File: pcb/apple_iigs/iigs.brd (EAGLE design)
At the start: 81 x 45 mm, 16 parts, among them J1 ATX24RH

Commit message: added iigs
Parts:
- removed C1, C2: (no value), capacitor-wima:C5B2.5
- removed JP3: (no value), appleii:1X04
- removed U$3: ROCK_SW, atx4vc:ROCK_SWITCH
- removed U$6: APPLEII, atx4vc:APPLEII
- added JP2: (no value), pinhead:1X03
- J1: device macse:ATX24_RIGHT_ANGLE -> appleii:ATX24_RIGHT_ANGLE
- moved J7 39.5 mm to (21.6, 4.23), turned to 0 degrees
- moved JP1 31.3 mm to (34.3, 5.57), turned to 0 degrees
- moved J1 28.7 mm to (3.00, 15.0), turned to 270 degrees
- moved U$1 25.2 mm to (31.3, 11.7)
- moved U$2 25.2 mm to (31.3, 19.5)
- moved U$4 22.8 mm to (51.5, 11.0)
- moved U$7 22.8 mm to (57.3, 15.0)
- moved JP4 18.8 mm to (44.3, 3.62)
- moved U$5 17.9 mm to (18.0, 11.0)
- moved IC1 11.8 mm to (27.7, 29.0)
- moved C3 11.7 mm to (38.7, 26.3)
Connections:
- new net N$1: JP2.2, JP4.2
- net +12V: now also JP2.3; no longer JP3.2, U$6.4
- net +5V: now also JP2.1; no longer JP4.2, U$6.3
- net -12V: no longer U$6.5
- net -5V: no longer U$6.6
- net GND: no longer C1.2, C2.2, JP3.1, U$3.P$1, U$3.P$3, U$6.1, U$6.2
- net N$5: no longer U$3.P$2, U$3.P$4
- net N$6: no longer C1.1
- net N$8: no longer C2.1
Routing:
- net N$5: track 103.7 -> 23.4 mm
- net N$6: track 93.8 -> 46.7 mm
- net -5V: track 70.9 -> 29.8 mm
- net +5V: track 67.5 -> 36.5 mm
- net +12V: track 71.0 -> 43.4 mm
- net N$8: track 84.8 -> 60.1 mm, vias 1 -> 0
- net N$1: track 0.00 -> 4.41 mm
- net -12V: track 81.7 -> 77.6 mm
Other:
- board size 81 x 45 mm -> 60 x 52 mm
- board text added: "Apple IIgs PicoPSU Adaptor"
- board text removed: "Apple II / II Plus / IIe / IIgs PicoPSU Adaptor"
- board text removed: "picoRC.com"

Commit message: updated IIGS design
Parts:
- removed J7: (no value), atx_power_control:SCREWTERMINAL-3.5MM-2-NS
- removed U$4, U$5: M2.5_MOUNTING_HOLE, appleii:M3_MOUNTING_HOLE_PACK
- moved JP4 19.1 mm to (28.7, 14.6)
- moved U$7 17.8 mm to (43.3, 26.0)
- moved JP1 16.6 mm to (19.7, 13.5)
- moved C3 13.3 mm to (31.2, 37.3)
- moved IC1 12.9 mm to (21.4, 40.3)
- moved U$1 12.3 mm to (27.3, 23.4)
- moved U$2 11.9 mm to (27.3, 30.8)
- moved JP2 11.4 mm to (37.0, 15.6), turned to 90 degrees
- moved J1 11.0 mm to (3.00, 26.0)
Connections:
- net GND: no longer J7.2
- net N$5: no longer J7.1
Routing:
- net GND: track 0.00 -> 18.2 mm
- net N$5: track 23.4 -> 6.03 mm
- net -12V: track 77.6 -> 64.7 mm
- net +12V: track 43.4 -> 31.4 mm
- net +5V: track 36.5 -> 29.0 mm
- net -5V: track 29.8 -> 22.3 mm
- net N$8: track 60.1 -> 52.7 mm
- net N$1: track 4.41 -> 11.2 mm
- net N$6: track 46.7 -> 44.8 mm
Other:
- board size 60 x 52 mm -> 46 x 52 mm
- board text added: "1uF"
- board text added: "5A FUSE"
- board text added: "Apple IIGS PicoPSU Adaptor"
- board text added: "PD1 dekuNukem APR2023"
- board text added: "PSW"
- board text removed: "Apple IIgs PicoPSU Adaptor"
- board text removed: "FUSE 5A MAX"
- board text removed: "PS_ON"
- board text removed: "PT1 dekuNukem DEC 2022"
- board text removed: "min 1uF"

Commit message: updated silkscreen and improved GND return
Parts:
- moved JP1 0.13 mm to (19.7, 13.4), turned to 180 degrees
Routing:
- net GND: track 18.2 -> 0.00 mm
- net N$5: track 6.03 -> 9.52 mm
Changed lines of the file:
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@@
 <text x="34.5462" y="18.256" size="1.4224" layer="25" distance="35" rot="R270" align="center">12</text>
 <text x="34.576" y="12.8932" size="1.778" layer="25" distance="35" align="center">5</text>
-<text x="20.86" y="35.0692" size="1.016" layer="25" distance="35" align="center">G</text>
-<text x="23.527" y="35.0692" size="1.016" layer="25" distance="35" align="center">-12</text>
-<text x="26.067" y="35.0692" size="1.016" layer="25" distance="35" align="center">-5</text>
+<text x="18.923" y="35.179" size="1.016" layer="25" distance="35" align="center">G</text>
+<text x="21.209" y="35.179" size="1.016" layer="25" distance="35" align="center">-12</text>
+<text x="23.876" y="35.179" size="1.016" layer="25" distance="35" align="center">-5</text>
 <text x="39.672" y="17.9242" size="1.778" layer="25" distance="35" align="center">G</text>
 <text x="39.672" y="13.8602" size="1.778" layer="25" distance="35" align="center">G</text>
@@
 <text x="39.5632" y="38.892" size="1.778" layer="25" distance="35" rot="R270" align="center">-5</text>
 <text x="39.1768" y="33.781" size="1.778" layer="25" distance="35" rot="R90" align="center">-12</text>
-<text x="15.994" y="13.727" size="1.4224" layer="25" rot="R270" align="center">PSW</text>
+<text x="16.121" y="13.473" size="1.4224" layer="25" rot="R270" align="center">PSW</text>
 <wire x1="44.095" y1="11.5" x2="19.04" y2="11.5" width="0.0762" layer="20"/>
 <wire x1="19.04" y1="11.5" x2="16.5" y2="8.96" width="0.0762" layer="20" curve="90"/>
@@
 <element name="U$1" library="atx_power_control" package="FUSE_HOLDER_3IN1" value="CAR_FUSE_HOLDER3IN1" x="27.322" y="23.368" smashed="yes" rot="R180"/>
 <element name="U$2" library="atx_power_control" package="FUSE_HOLDER_3IN1" value="CAR_FUSE_HOLDER3IN1" x="27.322" y="30.768" smashed="yes"/>
-<element name="JP1" library="pinhead" library_urn="urn:adsk.eagle:library:325" package="1X02" package3d_urn="urn:adsk.eagle:package:22435/2" value="" x="19.738" y="13.52" smashed="yes">
-<attribute name="POPULARITY" value="98" x="19.738" y="13.52" size="1.778" layer="27" display="off"/>
-<attribute name="VALUE" x="17.198" y="10.345" size="1.27" layer="27"/>
+<element name="JP1" library="pinhead" library_urn="urn:adsk.eagle:library:325" package="1X02" package3d_urn="urn:adsk.eagle:package:22435/2" value="" x="19.738" y="13.393" smashed="yes" rot="R180">
+<attribute name="POPULARITY" value="98" x="19.738" y="13.393" size="1.778" layer="27" rot="R180" display="off"/>
+<attribute name="VALUE" x="22.278" y="16.568" size="1.27" layer="27" rot="R180"/>
 </element>
 <element name="J1" library="appleii" package="ATX24_RIGHT_ANGLE" value="ATX24RH" x="3" y="26" smashed="yes" rot="R270"/>
@@
 <contactref element="U$7" pad="21"/>
 <contactref element="JP4" pad="1"/>
-<wire x1="33.782" y1="36.432" x2="33.782" y2="37.321" width="1.27" layer="1"/>
-<wire x1="33.782" y1="36.432" x2="32.402" y2="35.052" width="1.27" layer="1"/>
-<wire x1="18.9022" y1="37.716" x2="18.9022" y2="36.4698" width="1.27" layer="1"/>
-<wire x1="20.32" y1="35.052" x2="32.402" y2="35.052" width="1.27" layer="1"/>
-<wire x1="18.9022" y1="36.4698" x2="20.32" y2="35.052" width="1.27" layer="1"/>
+<polygon width="0.2032" layer="1" thermals="no">
+<vertex x="17.399" y="15.494"/>
+<vertex x="17.399" y="11.684"/>
+<vertex x="19.431" y="11.684"/>
+<vertex x="19.431" y="15.494"/>
+<vertex x="17.526" y="15.494"/>
+</polygon>
+<polygon width="0.2032" layer="1" thermals="no">
+<vertex x="17.78" y="39.751"/>
+<vertex x="20.066" y="39.751"/>
+<vertex x="20.066" y="35.814"/>
+<vertex x="17.78" y="35.814"/>
+</polygon>
+<polygon width="0.2032" layer="1" thermals="no">
+<vertex x="32.258" y="38.608"/>
+<vertex x="35.306" y="38.608"/>
+<vertex x="35.306" y="36.068"/>
+<vertex x="32.258" y="36.068"/>
+</polygon>
 </signal>
 <signal name="+5V">
@@
 <contactref element="JP1" pad="1"/>
 <contactref element="J1" pad="16"/>
-<wire x1="13.26" y1="15.5" x2="14.853" y2="15.5" width="0.6096" layer="16"/>
-<wire x1="16.833" y1="13.52" x2="18.468" y2="13.52" width="0.6096" layer="16"/>
-<wire x1="14.853" y1="15.5" x2="16.833" y2="13.52" width="0.6096" layer="16"/>
+<wire x1="13.26" y1="15.5" x2="20.441" y2="15.5" width="0.3048" layer="16"/>
+<wire x1="21.008" y1="14.933" x2="21.008" y2="13.393" width="0.3048" layer="16"/>
+<wire x1="20.441" y1="15.5" x2="21.008" y2="14.933" width="0.3048" layer="16"/>
 </signal>
 <signal name="-5V">

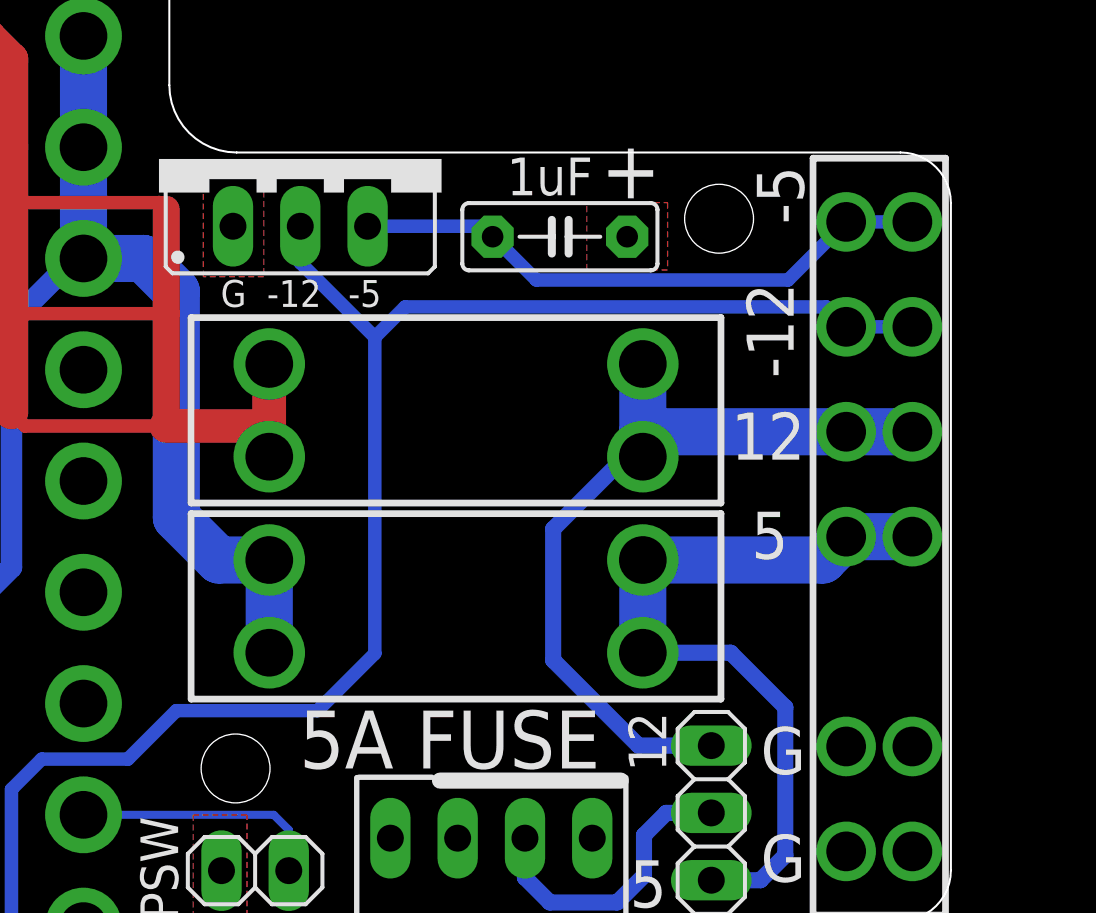
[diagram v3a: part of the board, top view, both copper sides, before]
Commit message: changed to 70L05
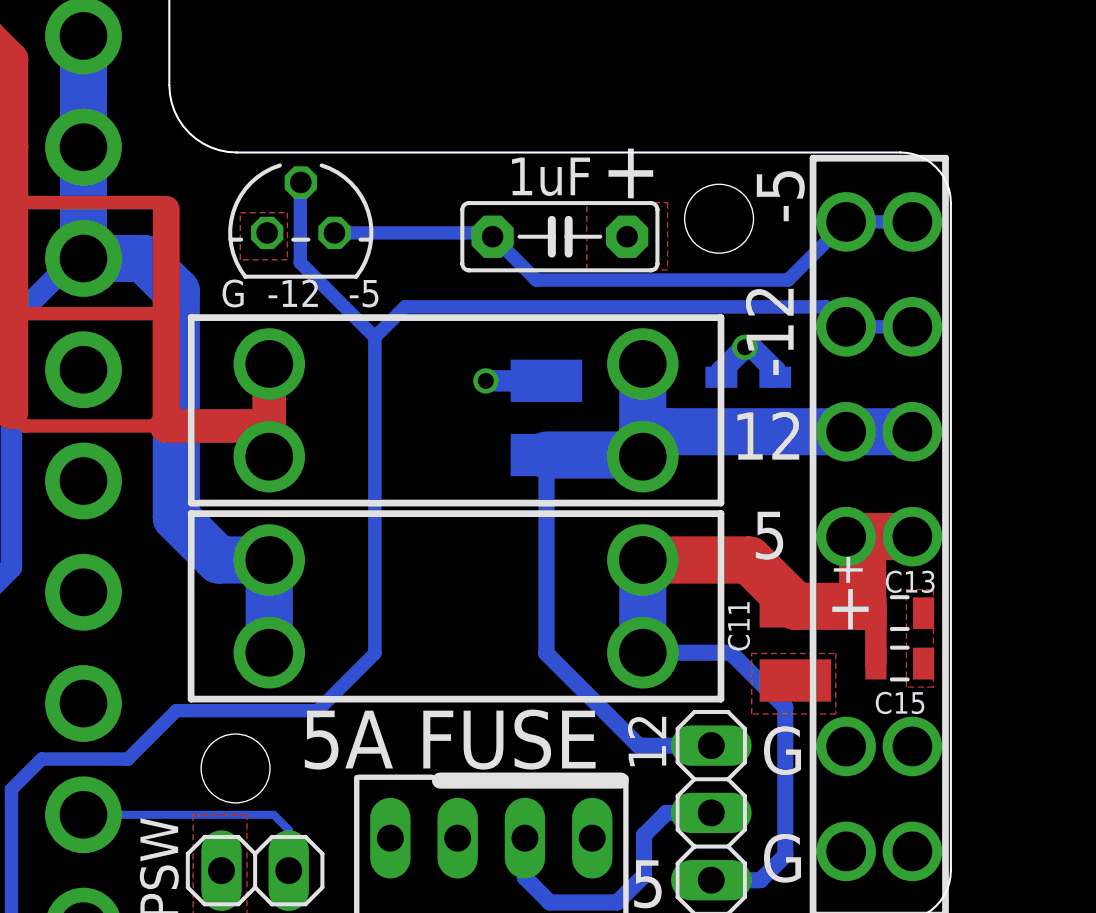
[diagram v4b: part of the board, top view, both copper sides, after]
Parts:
- removed IC1: (no value), v-reg:79XXS
- added C1, C11: 47uF, clock:C1210
- added C13, C15, C2, C4: 100nF, clock:0805@1
- added IC2: (no value), linear:TO92
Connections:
- net +12V: now also C1.1, C2.2, C4.2
- net +5V: now also C11.1, C13.2, C15.2
- net -12V: now also IC2.2; no longer IC1.IN
- net -5V: now also IC2.3; no longer IC1.OUT
- net GND: now also C1.2, C11.2, C13.1, C15.1, C2.1, C4.1, IC2.1; no longer IC1.GND
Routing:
- net +5V: track 29.0 -> 38.5 mm
- net +12V: track 31.4 -> 39.3 mm
- net GND: track 0.00 -> 5.55 mm, vias 0 -> 2
- net -12V: track 64.7 -> 66.4 mm
- net -5V: track 22.3 -> 23.5 mm

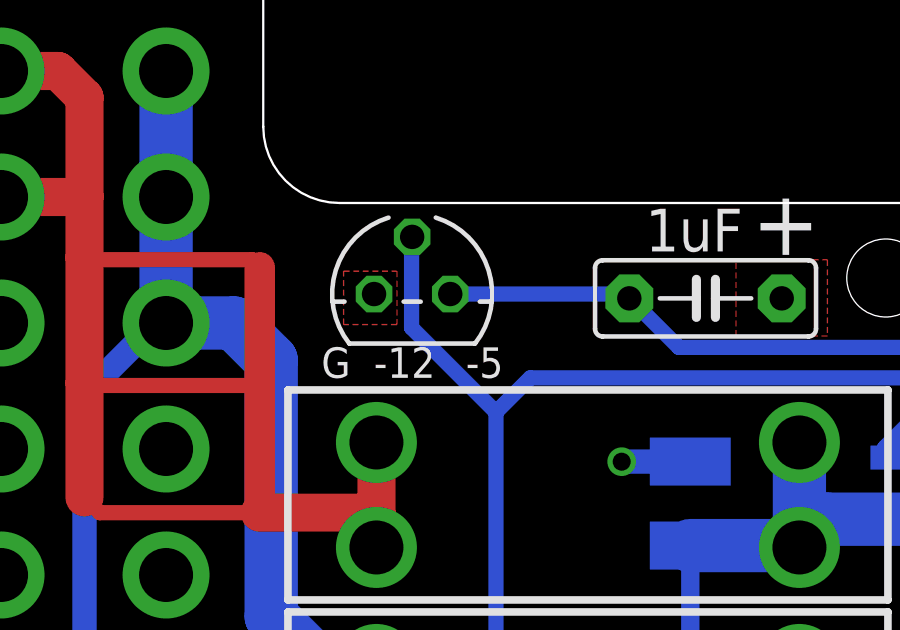
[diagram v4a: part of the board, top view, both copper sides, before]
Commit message: switched back to 7905
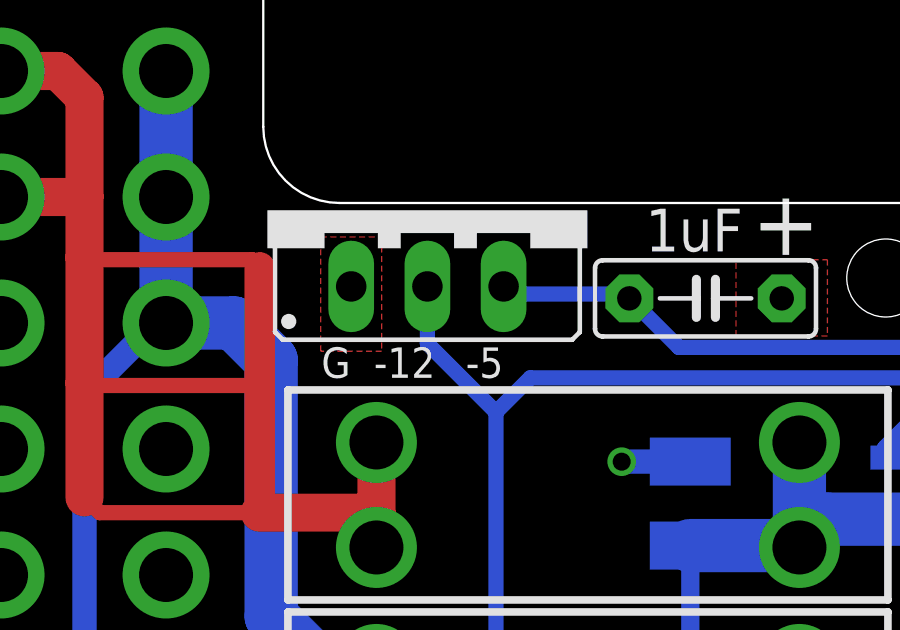
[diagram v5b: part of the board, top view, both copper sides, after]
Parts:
- removed IC2: (no value), linear:TO92
- added IC1: (no value), v-reg:79XXS
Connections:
- net -12V: now also IC1.IN; no longer IC2.2
- net -5V: now also IC1.OUT; no longer IC2.3
- net GND: now also IC1.GND; no longer IC2.1
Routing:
- net -12V: track 66.4 -> 64.5 mm
- net -5V: track 23.5 -> 21.8 mm
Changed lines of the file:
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@@
 <attribute name="VALUE" x="40.132" y="11.762" size="1.27" layer="27" rot="R90"/>
-</element>
-<element name="IC2" library="linear" library_urn="urn:adsk.eagle:library:262" package="TO92" package3d_urn="urn:adsk.eagle:package:16416/2" value="" x="21.463" y="37.465" smashed="yes">
-<attribute name="POPULARITY" value="0" x="21.463" y="37.465" size="1.778" layer="27" display="off"/>
-<attribute name="VALUE" x="24.384" y="36.195" size="1.27" layer="27" ratio="10"/>
 </element>
 <element name="C11" library="clock" package="C1210" value="47uF" x="40.132" y="21.971" smashed="yes" rot="R270">
@@
 <element name="C4" library="clock" package="0805@1" value="100nF" x="37.338" y="31.115" smashed="yes" rot="MR270">
 <attribute name="NAME" x="37.6555" y="33.782" size="0.8128" layer="26" rot="MR270"/>
+</element>
+<element name="IC1" library="v-reg" library_urn="urn:adsk.eagle:library:409" package="79XXS" package3d_urn="urn:adsk.eagle:package:30343/1" value="" x="21.971" y="40.259" smashed="yes">
+<attribute name="POPULARITY" value="3" x="21.971" y="41.275" size="1.778" layer="27" display="off"/>
+<attribute name="VALUE" x="16.891" y="32.639" size="1.27" layer="27" ratio="10"/>
 </element>
 </elements>
@@
 <vertex x="32.258" y="36.068"/>
 </polygon>
-<contactref element="IC2" pad="1"/>
 <contactref element="C15" pad="1"/>
 <contactref element="C13" pad="1"/>
@@
 <wire x1="39.37" y1="32.269" x2="38.492" y2="33.147" width="0.8128" layer="16"/>
 <polygon width="0.2032" layer="1" thermals="no">
-<vertex x="19.177" y="38.227"/>
-<vertex x="20.955" y="38.227"/>
-<vertex x="20.955" y="36.449"/>
-<vertex x="19.177" y="36.449"/>
+<vertex x="18.415" y="39.37"/>
+<vertex x="20.447" y="39.37"/>
+<vertex x="20.447" y="35.56"/>
+<vertex x="18.415" y="35.56"/>
 </polygon>
 <polygon width="0.2032" layer="1" thermals="no">
@@
 <vertex x="41.656" y="19.304"/>
 </polygon>
+<contactref element="IC1" pad="GND"/>
 </signal>
 <signal name="+5V">
@@
 <wire x1="14.937" y1="17.604" x2="16.764" y2="19.431" width="0.508" layer="16"/>
 <wire x1="24.257" y1="21.59" x2="24.257" y2="33.528" width="0.508" layer="16"/>
-<wire x1="24.257" y1="33.528" x2="21.4422" y2="36.3428" width="0.508" layer="16"/>
 <wire x1="24.257" y1="33.528" x2="25.4" y2="34.671" width="0.508" layer="16"/>
 <wire x1="41.296" y1="34.671" x2="42.047" y2="33.92" width="0.508" layer="16"/>
 <wire x1="25.4" y1="34.671" x2="41.296" y2="34.671" width="0.508" layer="16"/>
 <wire x1="42.047" y1="33.92" x2="44.547" y2="33.92" width="0.508" layer="16"/>
-<contactref element="IC2" pad="2"/>
-<wire x1="21.4422" y1="36.3428" x2="21.4422" y2="39.3492" width="0.508" layer="16"/>
-<wire x1="21.4422" y1="39.3492" x2="21.463" y2="39.37" width="0.508" layer="16"/>
+<contactref element="IC1" pad="IN"/>
+<wire x1="21.971" y1="37.719" x2="21.971" y2="35.814" width="0.508" layer="16"/>
+<wire x1="21.971" y1="35.814" x2="24.257" y2="33.528" width="0.508" layer="16"/>
 </signal>
 <signal name="N$6">
@@
 <wire x1="39.854" y1="35.687" x2="42.047" y2="37.88" width="0.508" layer="16"/>
 <wire x1="42.047" y1="37.88" x2="44.547" y2="37.88" width="0.508" layer="16"/>
-<contactref element="IC2" pad="3"/>
-<wire x1="22.733" y1="37.465" x2="28.558" y2="37.465" width="0.508" layer="16"/>
 <wire x1="28.558" y1="37.465" x2="28.702" y2="37.321" width="0.508" layer="16"/>
+<contactref element="IC1" pad="OUT"/>
+<wire x1="24.511" y1="37.719" x2="24.76499375" y2="37.465" width="0.508" layer="16"/>
+<wire x1="24.76499375" y1="37.465" x2="28.558" y2="37.465" width="0.508" layer="16"/>
 </signal>
 <signal name="N$1">
